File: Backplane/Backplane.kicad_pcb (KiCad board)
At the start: 2 copper layers, 129.5 x 120 mm, 392 parts

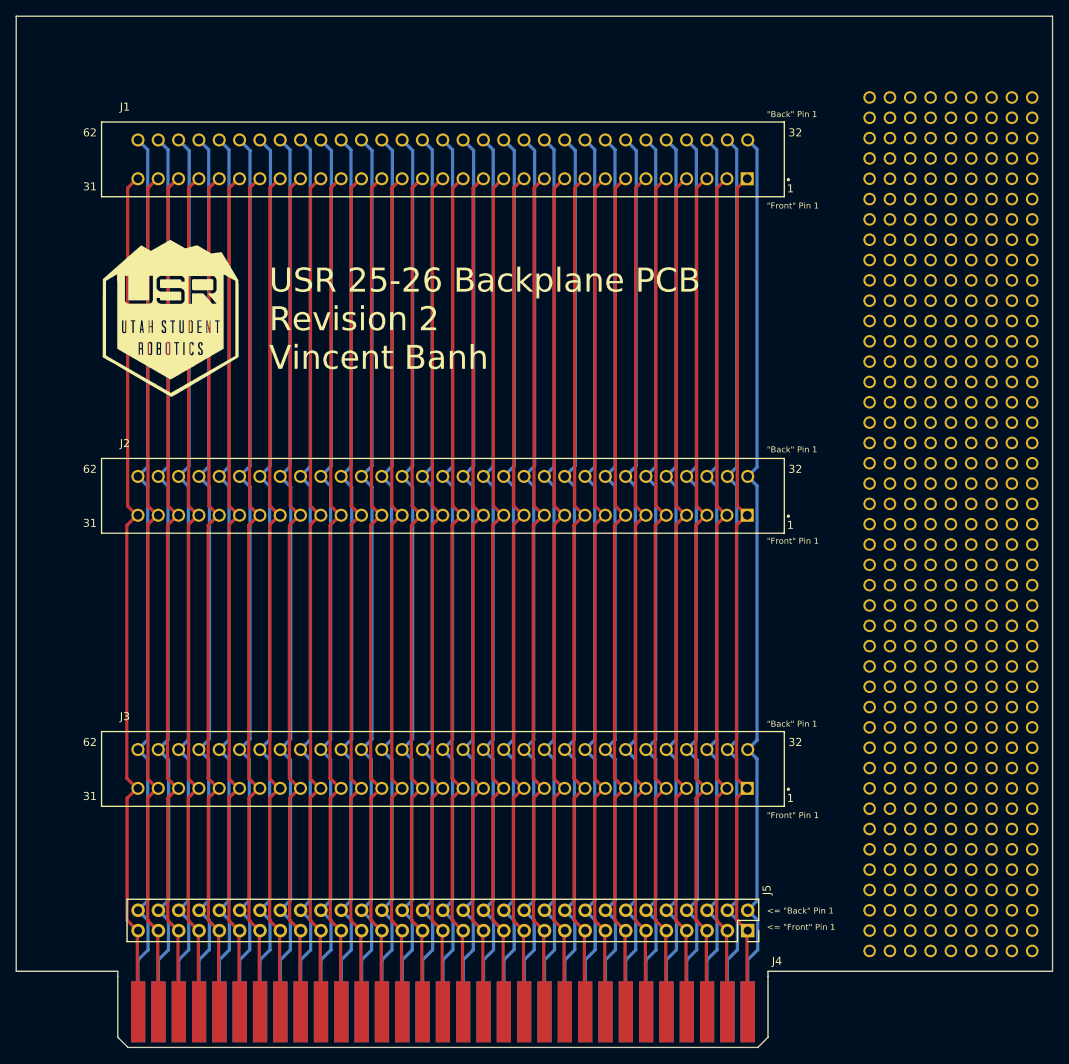
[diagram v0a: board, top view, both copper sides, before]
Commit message: added mounting holes to backplane
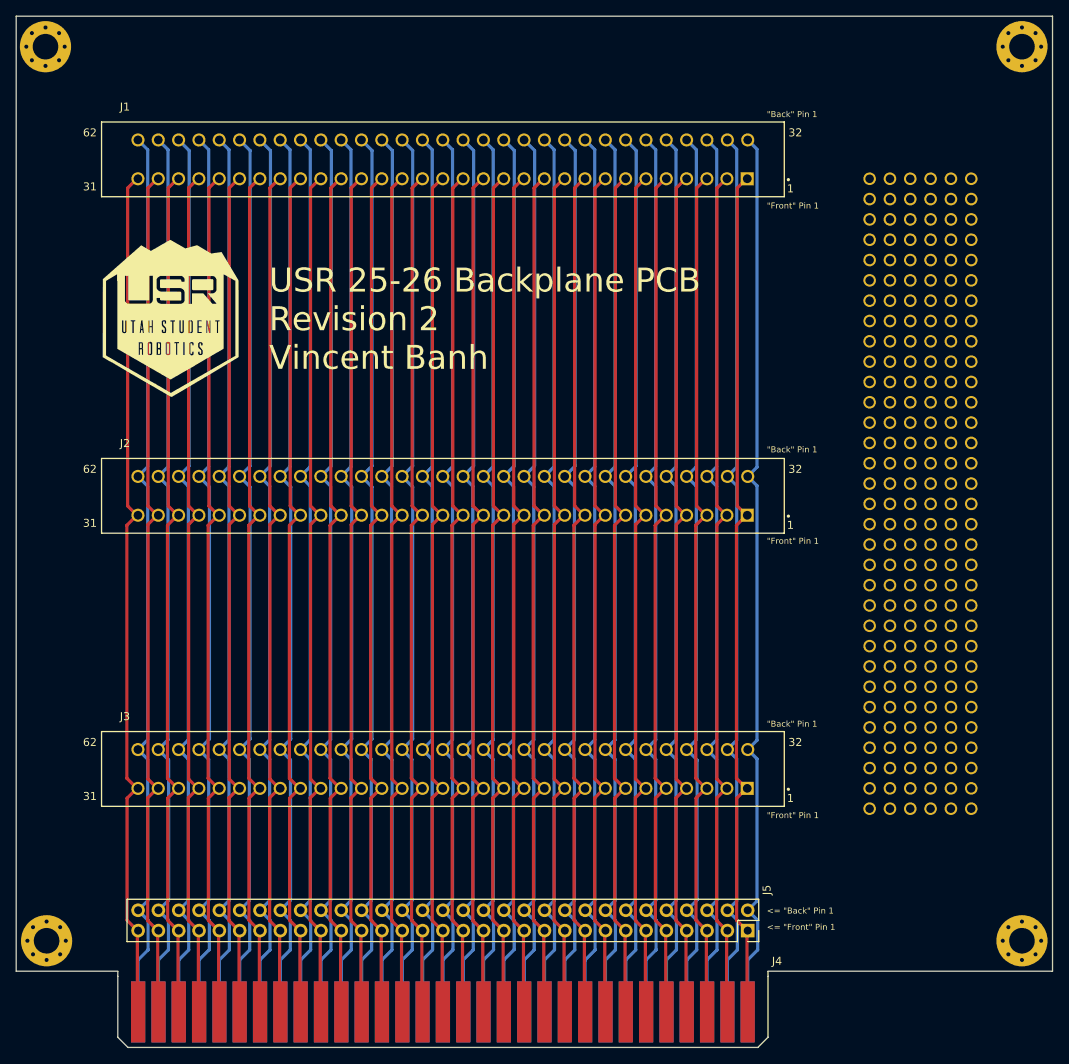
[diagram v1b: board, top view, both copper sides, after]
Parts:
- removed the ? at (186.8, 76.2)
- removed the ? at (184.3, 129.5)
- removed the ? at (171.6, 142.2)
- removed the ? at (179.2, 142.2)
- removed the ? at (179.2, 144.8)
- removed the ? at (186.8, 124.5)
- removed the ? at (191.9, 71.1)
- removed the ? at (189.4, 66.0)
- removed the ? at (186.8, 73.7)
- removed the ? at (179.2, 139.7)
- removed the ? at (189.4, 96.5)
- removed the ? at (189.4, 127.0)
- removed the ? at (189.4, 73.7)
- removed the ? at (186.8, 61.0)
- removed the ? at (186.8, 104.1)
- removed the ? at (189.4, 55.9)
- removed the ? at (186.8, 55.9)
- removed the ? at (176.7, 43.2)
- removed the ? at (191.9, 53.3)
- removed the ? at (179.2, 45.7)
- removed the ? at (176.7, 137.2)
- removed the ? at (184.3, 144.8)
- removed the ? at (186.8, 48.3)
- removed the ? at (189.4, 94.0)
- removed the ? at (191.9, 111.8)
- removed the ? at (181.8, 132.1)
- removed the ? at (186.8, 116.8)
- removed the ? at (189.4, 58.4)
- removed the ? at (191.9, 101.6)
- removed the ? at (189.4, 132.1)
- removed the ? at (171.6, 45.7)
- removed the ? at (191.9, 43.2)
- removed the ? at (189.4, 116.8)
- removed the ? at (171.6, 144.8)
- removed the ? at (191.9, 109.2)
- removed the ? at (186.8, 121.9)
- removed the ? at (184.3, 132.1)
- removed the ? at (181.8, 139.7)
- removed the ? at (191.9, 96.5)
- removed the ? at (184.3, 134.6)
- removed the ? at (171.6, 134.6)
- removed the ? at (179.2, 38.1)
- removed the ? at (174.1, 137.2)
- removed the ? at (176.7, 139.7)
- removed the ? at (191.9, 132.1)
- removed the ? at (186.8, 114.3)
- removed the ? at (179.2, 129.5)
- removed the ? at (181.8, 45.7)
- removed the ? at (186.8, 71.1)
- removed the ? at (189.4, 119.4)
- removed the ? at (186.8, 38.1)
- removed the ? at (186.8, 129.5)
- removed the ? at (174.1, 45.7)
- removed the ? at (186.8, 144.8)
- removed the ? at (191.9, 139.7)
- removed the ? at (179.2, 43.2)
- removed the ? at (171.6, 139.7)
- removed the ? at (189.4, 142.2)
- removed the ? at (189.4, 86.4)
- removed the ? at (186.8, 86.4)
- removed the ? at (184.3, 137.2)
- removed the ? at (191.9, 127.0)
- removed the ? at (176.7, 144.8)
- removed the ? at (181.8, 134.6)
- removed the ? at (189.4, 137.2)
- removed the ? at (186.8, 111.8)
- removed the ? at (186.8, 132.1)
- removed the ? at (181.8, 137.2)
- removed the ? at (176.7, 40.6)
- removed the ? at (191.9, 142.2)
- removed the ? at (191.9, 88.9)
- removed the ? at (191.9, 76.2)
- removed the ? at (189.4, 121.9)
- removed the ? at (174.1, 134.6)
- removed the ? at (184.3, 38.1)
- removed the ? at (179.2, 132.1)
- removed the ? at (191.9, 61.0)
- removed the ? at (174.1, 139.7)
- removed the ? at (181.8, 40.6)
- removed the ? at (191.9, 104.1)
- removed the ? at (189.4, 40.6)
- removed the ? at (186.8, 137.2)
- removed the ? at (186.8, 134.6)
- removed the ? at (186.8, 40.6)
- removed the ? at (189.4, 88.9)
- removed the ? at (186.8, 43.2)
- removed the ? at (179.2, 137.2)
- removed the ? at (191.9, 119.4)
- removed the ? at (181.8, 43.2)
- removed the ? at (184.3, 139.7)
- removed the ? at (174.1, 38.1)
- removed the ? at (174.1, 132.1)
- removed the ? at (176.7, 132.1)
- removed the ? at (186.8, 53.3)
- removed the ? at (189.4, 81.3)
- removed the ? at (186.8, 106.7)
- removed the ? at (191.9, 94.0)
- removed the ? at (186.8, 63.5)
- removed the ? at (184.3, 45.7)
- removed the ? at (181.8, 38.1)
- removed the ? at (191.9, 45.7)
- removed the ? at (186.8, 96.5)
- removed the ? at (174.1, 129.5)
- removed the ? at (189.4, 91.4)
- removed the ? at (189.4, 109.2)
- removed the ? at (174.1, 144.8)
- removed the ? at (179.2, 40.6)
- removed the ? at (186.8, 58.4)
- removed the ? at (189.4, 71.1)
- removed the ? at (184.3, 40.6)
- removed the ? at (191.9, 116.8)
- removed the ? at (171.6, 129.5)
- removed the ? at (174.1, 40.6)
- removed the ? at (189.4, 50.8)
- removed the ? at (171.6, 132.1)
- removed the ? at (189.4, 43.2)
- removed the ? at (191.9, 63.5)
- removed the ? at (186.8, 66.0)
- removed the ? at (171.6, 43.2)
- removed the ? at (186.8, 119.4)
- removed the ? at (191.9, 50.8)
- removed the ? at (186.8, 68.6)
- removed the ? at (184.3, 142.2)
- removed the ? at (191.9, 121.9)
- removed the ? at (176.7, 45.7)
- removed the ? at (191.9, 114.3)
- removed the ? at (186.8, 81.3)
- removed the ? at (176.7, 38.1)
- removed the ? at (189.4, 134.6)
- removed the ? at (191.9, 78.7)
- removed the ? at (186.8, 78.7)
- removed the ? at (171.6, 38.1)
- removed the ? at (179.2, 134.6)
- removed the ? at (189.4, 124.5)
- removed the ? at (191.9, 58.4)
- removed the ? at (191.9, 48.3)
- removed the ? at (181.8, 129.5)
- removed the ? at (191.9, 144.8)
- removed the ? at (184.3, 43.2)
- removed the ? at (189.4, 144.8)
- removed the ? at (191.9, 134.6)
- removed the ? at (176.7, 134.6)
- removed the ? at (191.9, 99.1)
- removed the ? at (186.8, 50.8)
- removed the ? at (191.9, 91.4)
- removed the ? at (191.9, 73.7)
- removed the ? at (189.4, 111.8)
- removed the ? at (191.9, 66.0)
- removed the ? at (176.7, 129.5)
- removed the ? at (189.4, 48.3)
- removed the ? at (186.8, 91.4)
- removed the ? at (186.8, 139.7)
- removed the ? at (189.4, 53.3)
- removed the ? at (191.9, 38.1)
- removed the ? at (191.9, 124.5)
- removed the ? at (189.4, 76.2)
- removed the ? at (189.4, 68.6)
- removed the ? at (186.8, 45.7)
- removed the ? at (191.9, 86.4)
- removed the ? at (186.8, 83.8)
- removed the ? at (181.8, 142.2)
- removed the ? at (189.4, 139.7)
- removed the ? at (186.8, 127.0)
- removed the ? at (171.6, 137.2)
- removed the ? at (191.9, 137.2)
- removed the ? at (189.4, 63.5)
- removed the ? at (186.8, 99.1)
- removed the ? at (191.9, 40.6)
- removed the ? at (186.8, 101.6)
- removed the ? at (189.4, 114.3)
- removed the ? at (186.8, 88.9)
- removed the ? at (181.8, 144.8)
- removed the ? at (189.4, 61.0)
- removed the ? at (191.9, 129.5)
- removed the ? at (191.9, 106.7)
- removed the ? at (191.9, 83.8)
- removed the ? at (176.7, 142.2)
- removed the ? at (189.4, 129.5)
- removed the ? at (189.4, 104.1)
- removed the ? at (189.4, 106.7)
- removed the ? at (186.8, 142.2)
- removed the ? at (191.9, 68.6)
- removed the ? at (189.4, 78.7)
- removed the ? at (174.1, 43.2)
- removed the ? at (171.6, 40.6)
- removed the ? at (174.1, 142.2)
- removed the ? at (189.4, 99.1)
- removed the ? at (186.8, 94.0)
- removed the ? at (189.4, 83.8)
- removed the ? at (191.9, 81.3)
- removed the ? at (189.4, 45.7)
- removed the ? at (189.4, 101.6)
- removed the ? at (191.9, 55.9)
- removed the ? at (189.4, 38.1)
- removed the ? at (186.8, 109.2)
- added REF**: MountingHole_3.2mm_M3_Pad_Via, MountingHole:MountingHole_3.2mm_M3_Pad_Via, F.Cu at (68.6, 31.8)
- added REF**: MountingHole_3.2mm_M3_Pad_Via, MountingHole:MountingHole_3.2mm_M3_Pad_Via, F.Cu at (190.6, 143.5)
- added REF**: MountingHole_3.2mm_M3_Pad_Via, MountingHole:MountingHole_3.2mm_M3_Pad_Via, F.Cu at (68.7, 143.5)
- added REF**: MountingHole_3.2mm_M3_Pad_Via, MountingHole:MountingHole_3.2mm_M3_Pad_Via, F.Cu at (190.6, 31.8)
